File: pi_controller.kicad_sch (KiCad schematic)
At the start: 159 parts, among them J1 PWM, J17 CS2, J18 CS4, J19 CS6, J2 DC Supply, J20 CS8, J21 CS3, J22 CS5, J23 CS7, J26 LED6, J27 LED5, J28 LED7, J29 LED8, J30 I2C, J31 UART, J32 LED3, J33 LED1, J34 LED2, J35 LED4, J36 ROW1, J37 ROW2, J38 ROW3, J39 ROW5, J40 ROW4, J41 ROW6, J42 ROW7, J43 ROW8, Q1 AOD4184A, Q2 MMBT3904, U1 AP62300TWU, U2 CD74HC4067SM96, U3 LM4040DBZ-3, U4 RaspberryPi_Pico, U5 74HC138, U6 TM1639 (TA2009B), U7 74HC138

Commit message: Adjusting components
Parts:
- AN1, AN10, AN11, AN12, AN13, AN14, AN15, AN16, AN2, AN3, AN4, AN5, AN6, AN7, AN8, AN9, J1: JLCPCB Part # (none) -> C49257
- renumbered J36 to JR1, J37 to JR2, J38 to JR3, J40 to JR4, J39 to JR5, J41 to JR6, J42 to JR7, J43 to JR8
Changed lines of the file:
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@@
 		(dnp no)
 		(fields_autoplaced yes)
-		(property "Reference" "J42"
+		(property "Reference" "JR7"
 			(at 462.28 233.6799 90)
 			(effects
@@
 			(project "pi_controller"
 				(path "/7937d148-dd0e-48a9-9446-42d1f47999d5"
-					(reference "J42")
+					(reference "JR7")
 					(unit 1)
 				)
@@
 			)
 		)
+		(property "JLCPCB Part #" "C49257"
+			(at 513.08 118.11 0)
+			(effects
+				(font
+					(size 1.27 1.27)
+				)
+				(hide yes)
+			)
+		)
 		(pin "1"
 		)
@@
 			)
 		)
+		(property "JLCPCB Part #" "C49257"
+			(at 535.94 152.4 0)
+			(effects
+				(font
+					(size 1.27 1.27)
+				)
+				(hide yes)
+			)
+		)
 		(pin "1"
 		)
@@
 			)
 		)
+		(property "JLCPCB Part #" "C49257"
+			(at 513.08 85.09 0)
+			(effects
+				(font
+					(size 1.27 1.27)
+				)
+				(hide yes)
+			)
+		)
 		(pin "1"
 		)
@@
 			)
 		)
+		(property "JLCPCB Part #" "C49257"
+			(at 513.08 152.4 0)
+			(effects
+				(font
+					(size 1.27 1.27)
+				)
+				(hide yes)
+			)
+		)
 		(pin "1"
 		)
@@
 			)
 		)
+		(property "JLCPCB Part #" "C49257"
+			(at 535.94 85.09 0)
+			(effects
+				(font
+					(size 1.27 1.27)
+				)
+				(hide yes)
+			)
+		)
 		(pin "1"
 		)
@@
 			)
 		)
+		(property "JLCPCB Part #" "C49257"
+			(at 513.08 168.91 0)
+			(effects
+				(font
+					(size 1.27 1.27)
+				)
+				(hide yes)
+			)
+		)
 		(pin "1"
 		)
@@
 		(dnp no)
 		(fields_autoplaced yes)
-		(property "Reference" "J39"
+		(property "Reference" "JR5"
 			(at 373.38 274.3199 90)
 			(effects
@@
 			(project "pi_controller"
 				(path "/7937d148-dd0e-48a9-9446-42d1f47999d5"
-					(reference "J39")
+					(reference "JR5")
 					(unit 1)
 				)
@@
 			)
 		)
+		(property "JLCPCB Part #" "C49257"
+			(at 535.94 101.6 0)
+			(effects
+				(font
+					(size 1.27 1.27)
+				)
+				(hide yes)
+			)
+		)
 		(pin "1"
 		)
@@
 		(dnp no)
 		(fields_autoplaced yes)
-		(property "Reference" "J38"
+		(property "Reference" "JR3"
 			(at 285.75 317.4999 90)
 			(effects
@@
 			(project "pi_controller"
 				(path "/7937d148-dd0e-48a9-9446-42d1f47999d5"
-					(reference "J38")
+					(reference "JR3")
 					(unit 1)
 				)
@@
 			)
 		)
+		(property "JLCPCB Part #" "C49257"
+			(at 535.94 118.11 0)
+			(effects
+				(font
+					(size 1.27 1.27)
+				)
+				(hide yes)
+			)
+		)
 		(pin "1"
 		)
@@
 			)
 		)
+		(property "JLCPCB Part #" "C49257"
+			(at 513.08 135.89 0)
+			(effects
+				(font
+					(size 1.27 1.27)
+				)
+				(hide yes)
+			)
+		)
 		(pin "1"
 		)
@@
 			)
 		)
+		(property "JLCPCB Part #" "C49257"
+			(at 513.08 68.58 0)
+			(effects
+				(font
+					(size 1.27 1.27)
+				)
+				(hide yes)
+			)
+		)
 		(pin "1"
 		)
@@
 			)
 		)
+		(property "JLCPCB Part #" "C49257"
+			(at 513.08 101.6 0)
+			(effects
+				(font
+					(size 1.27 1.27)
+				)
+				(hide yes)
+			)
+		)
 		(pin "1"
 		)
@@
 		)
 		(property "Package" "0603"
-			(at 80.01 148.59 0)
+			(at 75.438 152.654 0)
 			(effects
 				(font
 					(size 1.27 1.27)
 				)
-				(hide yes)
 			)
 		)
 		(property "Power" "100mW"
-			(at 80.01 148.59 0)
+			(at 74.676 150.622 0)
 			(effects
 				(font
 					(size 1.27 1.27)
 				)
-				(hide yes)
 			)
 		)
 		(property "Tolerance" "1%"
-			(at 80.01 148.59 0)
+			(at 76.708 154.686 0)
 			(effects
 				(font
 					(size 1.27 1.27)
 				)
-				(hide yes)
 			)
 		)
@@
 			)
 		)
+		(property "JLCPCB Part #" "C49257"
+			(at 535.94 68.58 0)
+			(effects
+				(font
+					(size 1.27 1.27)
+				)
+				(hide yes)
+			)
+		)
 		(pin "1"
 		)
@@
 			)
 		)
+		(property "JLCPCB Part #" "C49257"
+			(at 535.94 135.89 0)
+			(effects
+				(font
+					(size 1.27 1.27)
+				)
+				(hide yes)
+			)
+		)
 		(pin "1"
 		)
@@
 			)
 		)
+		(property "JLCPCB Part #" "C49257"
+			(at 535.94 168.91 0)
+			(effects
+				(font
+					(size 1.27 1.27)
+				)
+				(hide yes)
+			)
+		)
 		(pin "1"
 		)
@@
 		(on_board yes)
 		(dnp no)
-		(fields_autoplaced yes)
-		(property "Reference" "J43"
+		(property "Reference" "JR8"
 			(at 462.28 275.5899 90)
 			(effects
@@
 			(project "pi_controller"
 				(path "/7937d148-dd0e-48a9-9446-42d1f47999d5"
-					(reference "J43")
+					(reference "JR8")
 					(unit 1)
 				)
@@
 		(dnp no)
 		(fields_autoplaced yes)
-		(property "Reference" "J37"
+		(property "Reference" "JR2"
 			(at 285.75 274.3199 90)
 			(effects
@@
 			(project "pi_controller"
 				(path "/7937d148-dd0e-48a9-9446-42d1f47999d5"
-					(reference "J37")
+					(reference "JR2")
 					(unit 1)
 				)
@@
 		(dnp no)
 		(fields_autoplaced yes)
-		(property "Reference" "J36"
+		(property "Reference" "JR1"
 			(at 285.75 232.4099 90)
 			(effects
@@
 			(project ""
 				(path "/7937d148-dd0e-48a9-9446-42d1f47999d5"
-					(reference "J36")
+					(reference "JR1")
 					(unit 1)
 				)
@@
 			)
 		)
+		(property "JLCPCB Part #" "C49257"
+			(at 513.08 50.8 0)
+			(effects
+				(font
+					(size 1.27 1.27)
+				)
+				(hide yes)
+			)
+		)
 		(pin "1"
 		)
@@
 		(dnp no)
 		(fields_autoplaced yes)
-		(property "Reference" "J41"
+		(property "Reference" "JR6"
 			(at 373.38 317.4999 90)
 			(effects
@@
 			(project "pi_controller"
 				(path "/7937d148-dd0e-48a9-9446-42d1f47999d5"
-					(reference "J41")
+					(reference "JR6")
 					(unit 1)
 				)
@@
 		(dnp no)
 		(fields_autoplaced yes)
-		(property "Reference" "J40"
+		(property "Reference" "JR4"
 			(at 373.38 232.4099 90)
 			(effects
@@
 			(project "pi_controller"
 				(path "/7937d148-dd0e-48a9-9446-42d1f47999d5"
-					(reference "J40")
+					(reference "JR4")
 					(unit 1)
 				)
@@
 			)
 		)
+		(property "JLCPCB Part #" "C49257"
+			(at 535.94 50.8 0)
+			(effects
+				(font
+					(size 1.27 1.27)
+				)
+				(hide yes)
+			)
+		)
 		(pin "1"
 		)
@@
 			(at 148.59 125.73 0)
 			(effects
+				(font
+					(size 1.27 1.27)
+				)
+				(hide yes)
+			)
+		)
+		(property "JLCPCB Part #" "C49257"
+			(at 148.59 125.73 0)
+			(effects

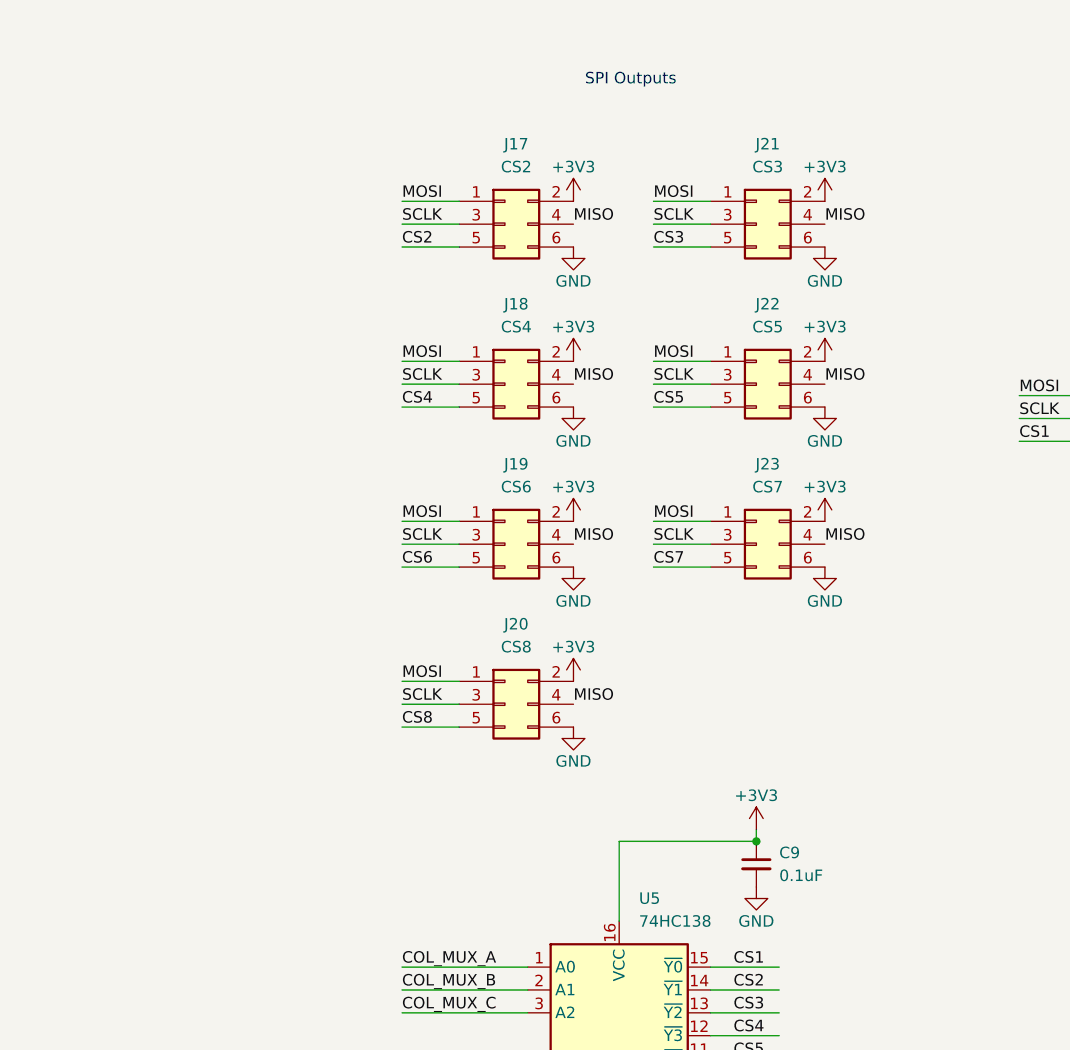
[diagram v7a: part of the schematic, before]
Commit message: New connectos and adjusted component spacing
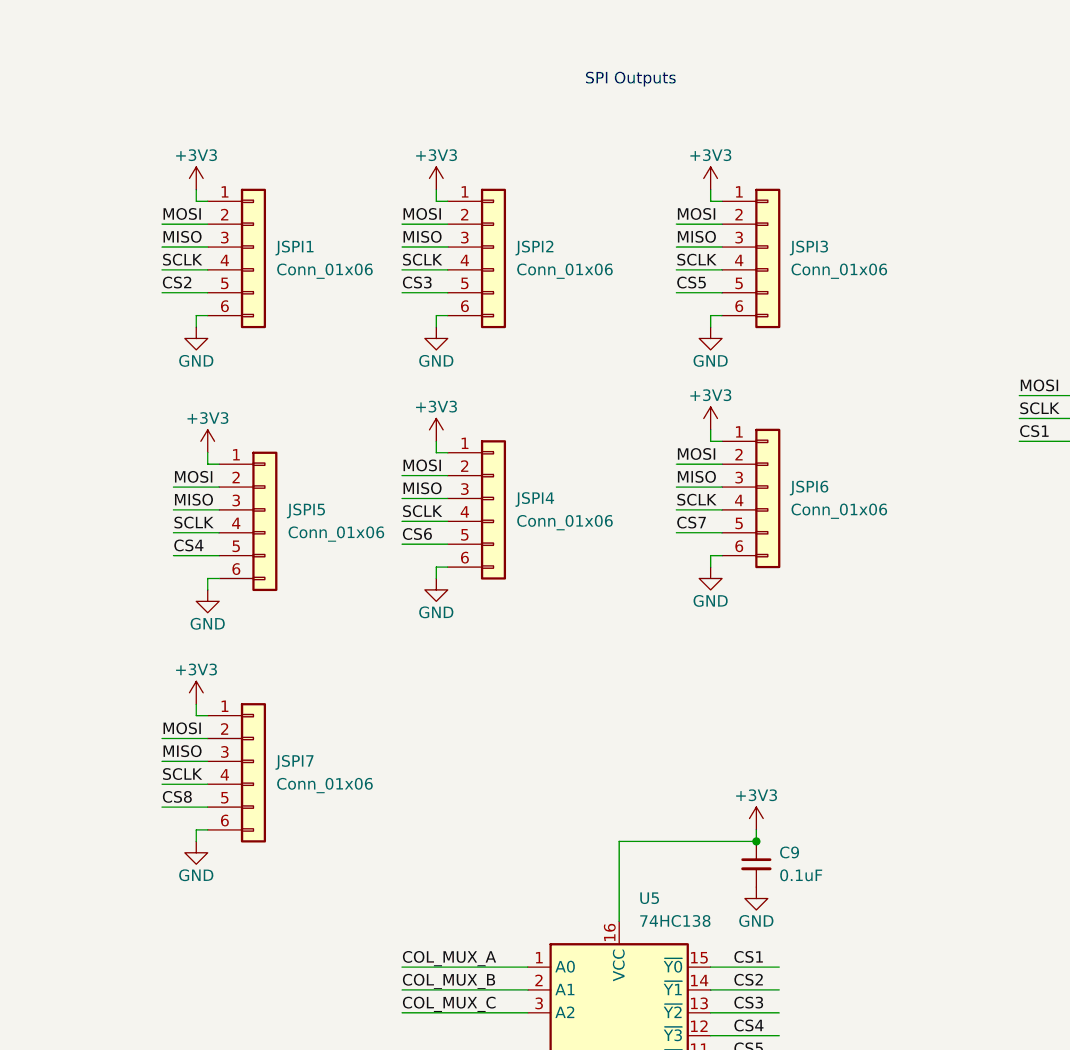
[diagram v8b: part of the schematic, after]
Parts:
- removed J17: CS2, Connector_PinHeader_2.54mm:PinHeader_2x03_P2.54mm_Vertical, symbol Connector_Generic:Conn_02x03_Odd_Even
- removed J18: CS4, Connector_PinHeader_2.54mm:PinHeader_2x03_P2.54mm_Vertical, symbol Connector_Generic:Conn_02x03_Odd_Even
- removed J19: CS6, Connector_PinHeader_2.54mm:PinHeader_2x03_P2.54mm_Vertical, symbol Connector_Generic:Conn_02x03_Odd_Even
- removed J20: CS8, Connector_PinHeader_2.54mm:PinHeader_2x03_P2.54mm_Vertical, symbol Connector_Generic:Conn_02x03_Odd_Even
- removed J21: CS3, Connector_PinHeader_2.54mm:PinHeader_2x03_P2.54mm_Vertical, symbol Connector_Generic:Conn_02x03_Odd_Even
- removed J22: CS5, Connector_PinHeader_2.54mm:PinHeader_2x03_P2.54mm_Vertical, symbol Connector_Generic:Conn_02x03_Odd_Even
- removed J23: CS7, Connector_PinHeader_2.54mm:PinHeader_2x03_P2.54mm_Vertical, symbol Connector_Generic:Conn_02x03_Odd_Even
- added JSPI1, JSPI2, JSPI3, JSPI4, JSPI5, JSPI6, JSPI7: Conn_01x06, PiMatrix:JST_ZH_B6B-ZR_1x06_P1.50mm_Vertical_SilkSafe, symbol Connector_Generic:Conn_01x06
- AN1, AN10, AN11, AN12, AN13, AN14, AN15, AN16, AN2, AN3, AN4, AN5, AN6, AN7, AN8, AN9: footprint Connector_PinHeader_2.54mm:PinHeader_1x03_P2.54mm_Vertical -> PiMatrix:JST_ZH_B3B-ZR_1x03_P1.50mm_Vertical_SilkSafe; JLCPCB Part # C49257 -> C495558
- J30, J31: footprint Connector_PinHeader_2.54mm:PinHeader_1x04_P2.54mm_Vertical -> PiMatrix:JST_ZH_B4B-ZR_1x04_P1.50mm_Vertical_SilkSafe; JLCPCB Part # (none) -> C163034
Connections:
- net +3V3: now also JSPI1.1 (Pin_1), JSPI2.1 (Pin_1), JSPI3.1 (Pin_1), JSPI4.1 (Pin_1), JSPI5.1 (Pin_1), JSPI6.1 (Pin_1), JSPI7.1 (Pin_1)
- net CS2: now also JSPI1.5 (Pin_5)
- net CS3: now also JSPI2.5 (Pin_5)
- net CS4: now also JSPI5.5 (Pin_5)
- net CS5: now also JSPI3.5 (Pin_5)
- net CS6: now also JSPI4.5 (Pin_5)
- net CS7: now also JSPI6.5 (Pin_5)
- net CS8: now also JSPI7.5 (Pin_5)
- net GND: now also JSPI1.6 (Pin_6), JSPI2.6 (Pin_6), JSPI3.6 (Pin_6), JSPI4.6 (Pin_6), JSPI5.6 (Pin_6), JSPI6.6 (Pin_6), JSPI7.6 (Pin_6)
- net MISO: now also JSPI1.3 (Pin_3), JSPI2.3 (Pin_3), JSPI3.3 (Pin_3), JSPI4.3 (Pin_3), JSPI5.3 (Pin_3), JSPI6.3 (Pin_3), JSPI7.3 (Pin_3)
- net MOSI: now also JSPI1.2 (Pin_2), JSPI2.2 (Pin_2), JSPI3.2 (Pin_2), JSPI4.2 (Pin_2), JSPI5.2 (Pin_2), JSPI6.2 (Pin_2), JSPI7.2 (Pin_2)
- net SCLK: now also JSPI1.4 (Pin_4), JSPI2.4 (Pin_4), JSPI3.4 (Pin_4), JSPI4.4 (Pin_4), JSPI5.4 (Pin_4), JSPI6.4 (Pin_4), JSPI7.4 (Pin_4)
